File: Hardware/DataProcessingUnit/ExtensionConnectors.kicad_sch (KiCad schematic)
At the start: 1 part

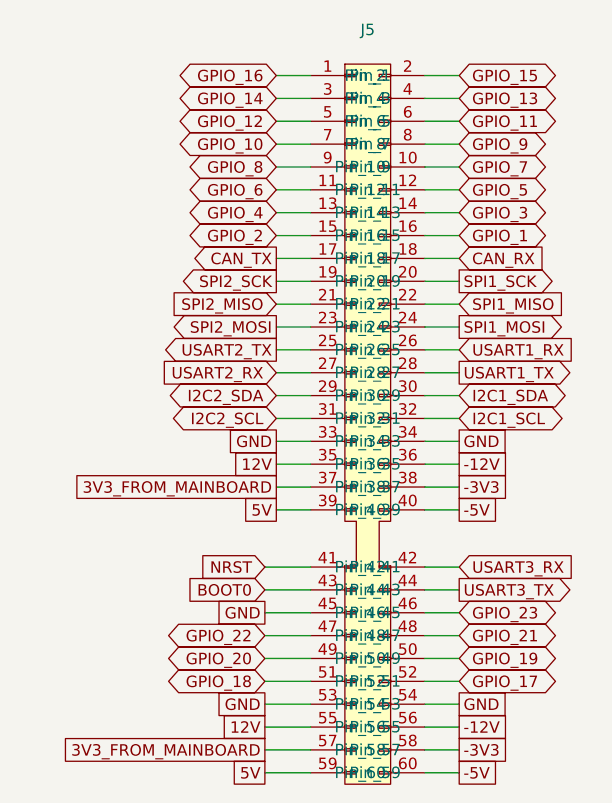
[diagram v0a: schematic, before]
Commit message: rework CI, make PCB smaller
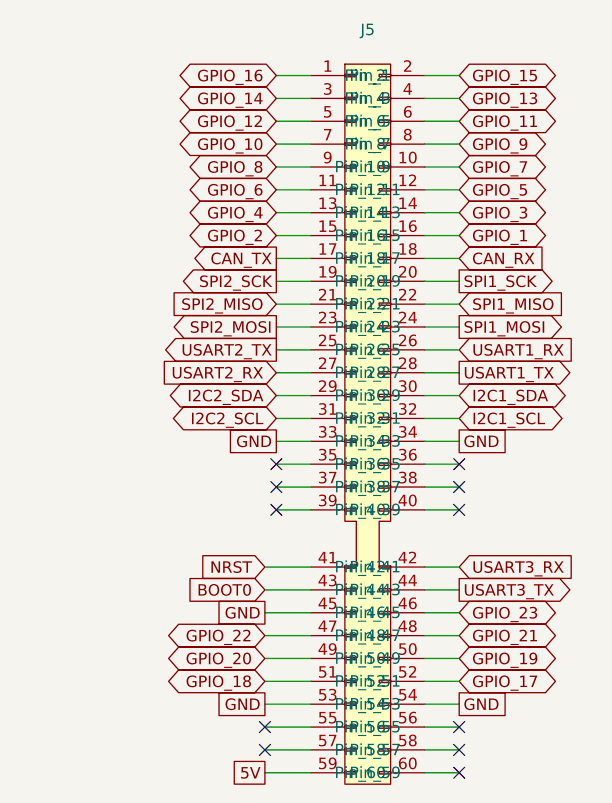
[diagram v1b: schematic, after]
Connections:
- net 5V: no longer J5.39 (Pin_39)
- net -12V: no longer names the net of J5.36 (Pin_36)
- net -12V: no longer J5.56 (Pin_56)
- net -3V3: no longer names the net of J5.38 (Pin_38)
- net -3V3: no longer J5.58 (Pin_58)
- net -5V: no longer names the net of J5.40 (Pin_40)
- net -5V: no longer J5.60 (Pin_60)
- net 12V: no longer names the net of J5.35 (Pin_35)
- net 12V: no longer J5.55 (Pin_55)
- net 3V3_FROM_MAINBOARD: no longer names the net of J5.37 (Pin_37)
- net 3V3_FROM_MAINBOARD: no longer J5.57 (Pin_57)
- no-connect marks 0 -> 11
